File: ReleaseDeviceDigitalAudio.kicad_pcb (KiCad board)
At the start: 4 copper layers, 132 x 68.5 mm, 179 parts, among them J1 Conn_02x10_Counter_Clockwise, J2 ATMEGA_PROG, J3 SignalStrength, J4 UIBoardCON1, J5 Conn_01x04, J6 UIBoardCON2, J7 KeySwitch, Q1 BSS314PEH6327XTSA1, Q3 SQ2362ES-T1_GE3, Q4 SQD50P06-15L_GE3, U1 ATmega4809-A, U10 ULN2003F12FN-7, U11 ULN2003F12FN-7, U12 ULN2003F12FN-7, U13 ULN2003F12FN-7, U14 MAX98089ETN+, U15 SN74LV1T126, U16 SN74LV1T126, U17 BM83SM1-00TA, U18 PCF85063A, U2 VOMA617A, U3 VOMA617A, U4 LM53635LQRNL*Q1, U5 TLVH431AQDBVRQ1, U6 LM74610-Q1, U7 Compute_Module_4_Connectors, U8 CD4514BM, U9 CD4511BPWR, Y1 9HT12

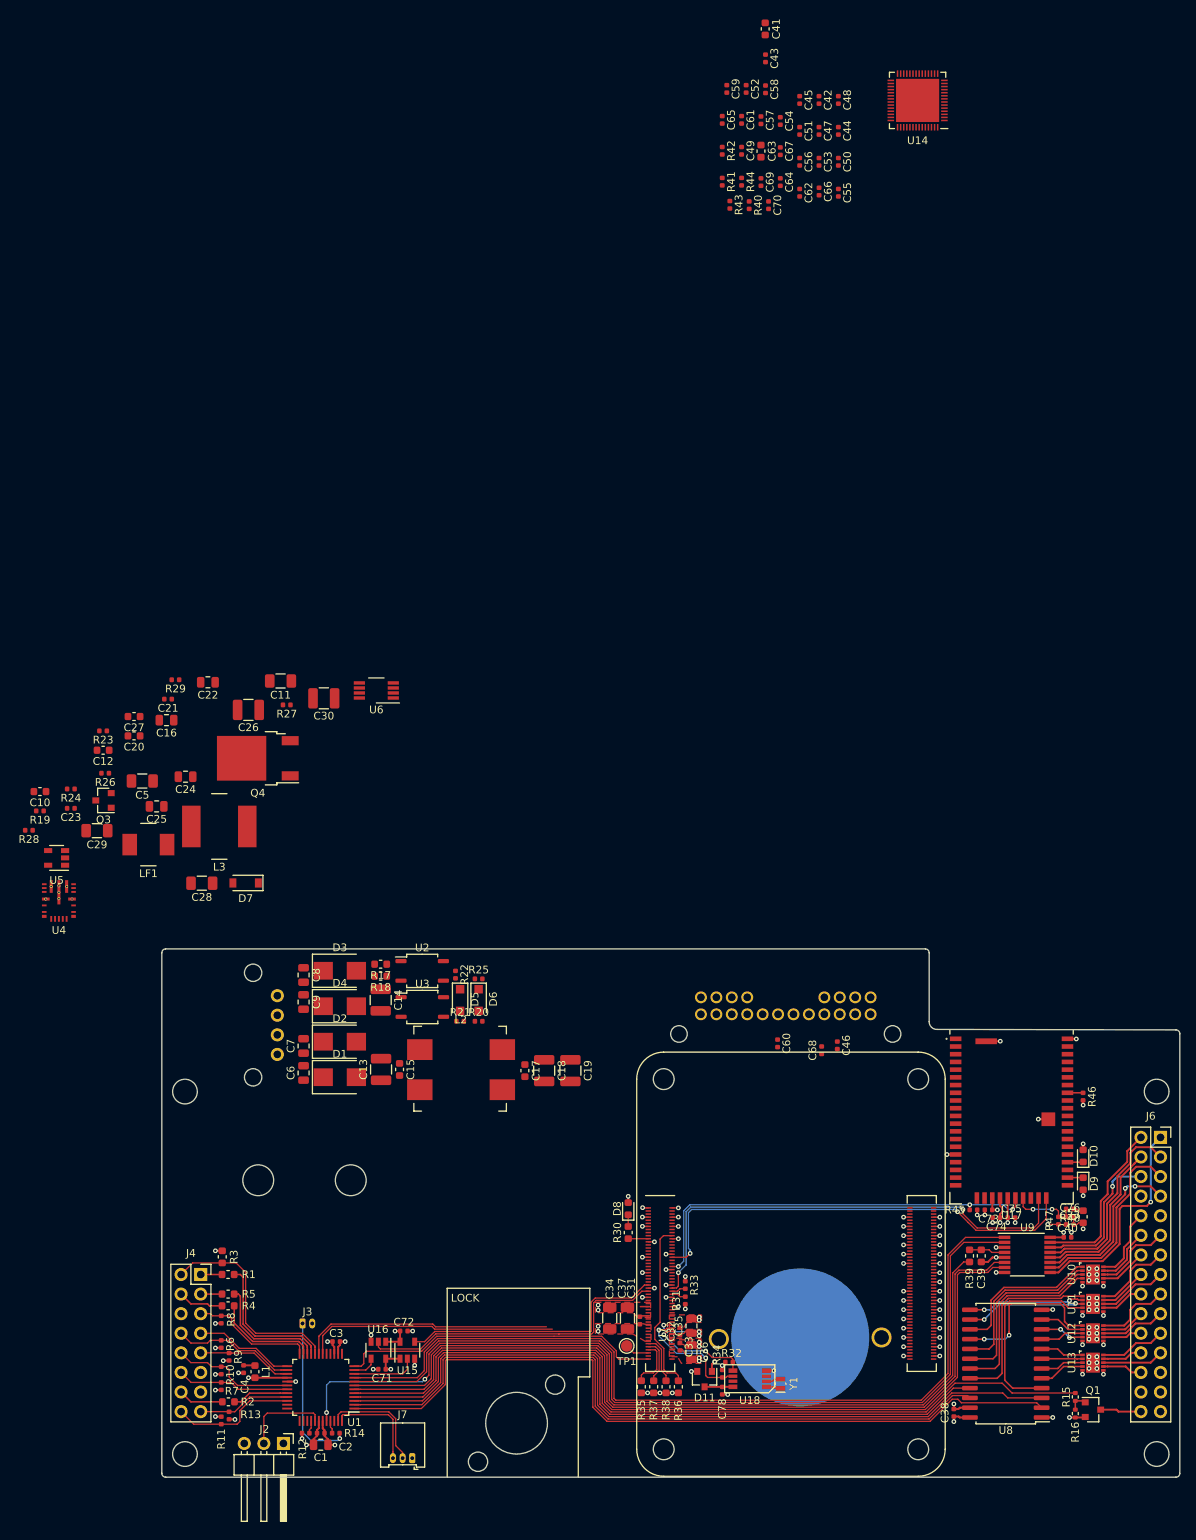
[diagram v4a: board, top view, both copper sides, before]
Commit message: - Layout MAX98 - Audiostecker Belegung angepasst
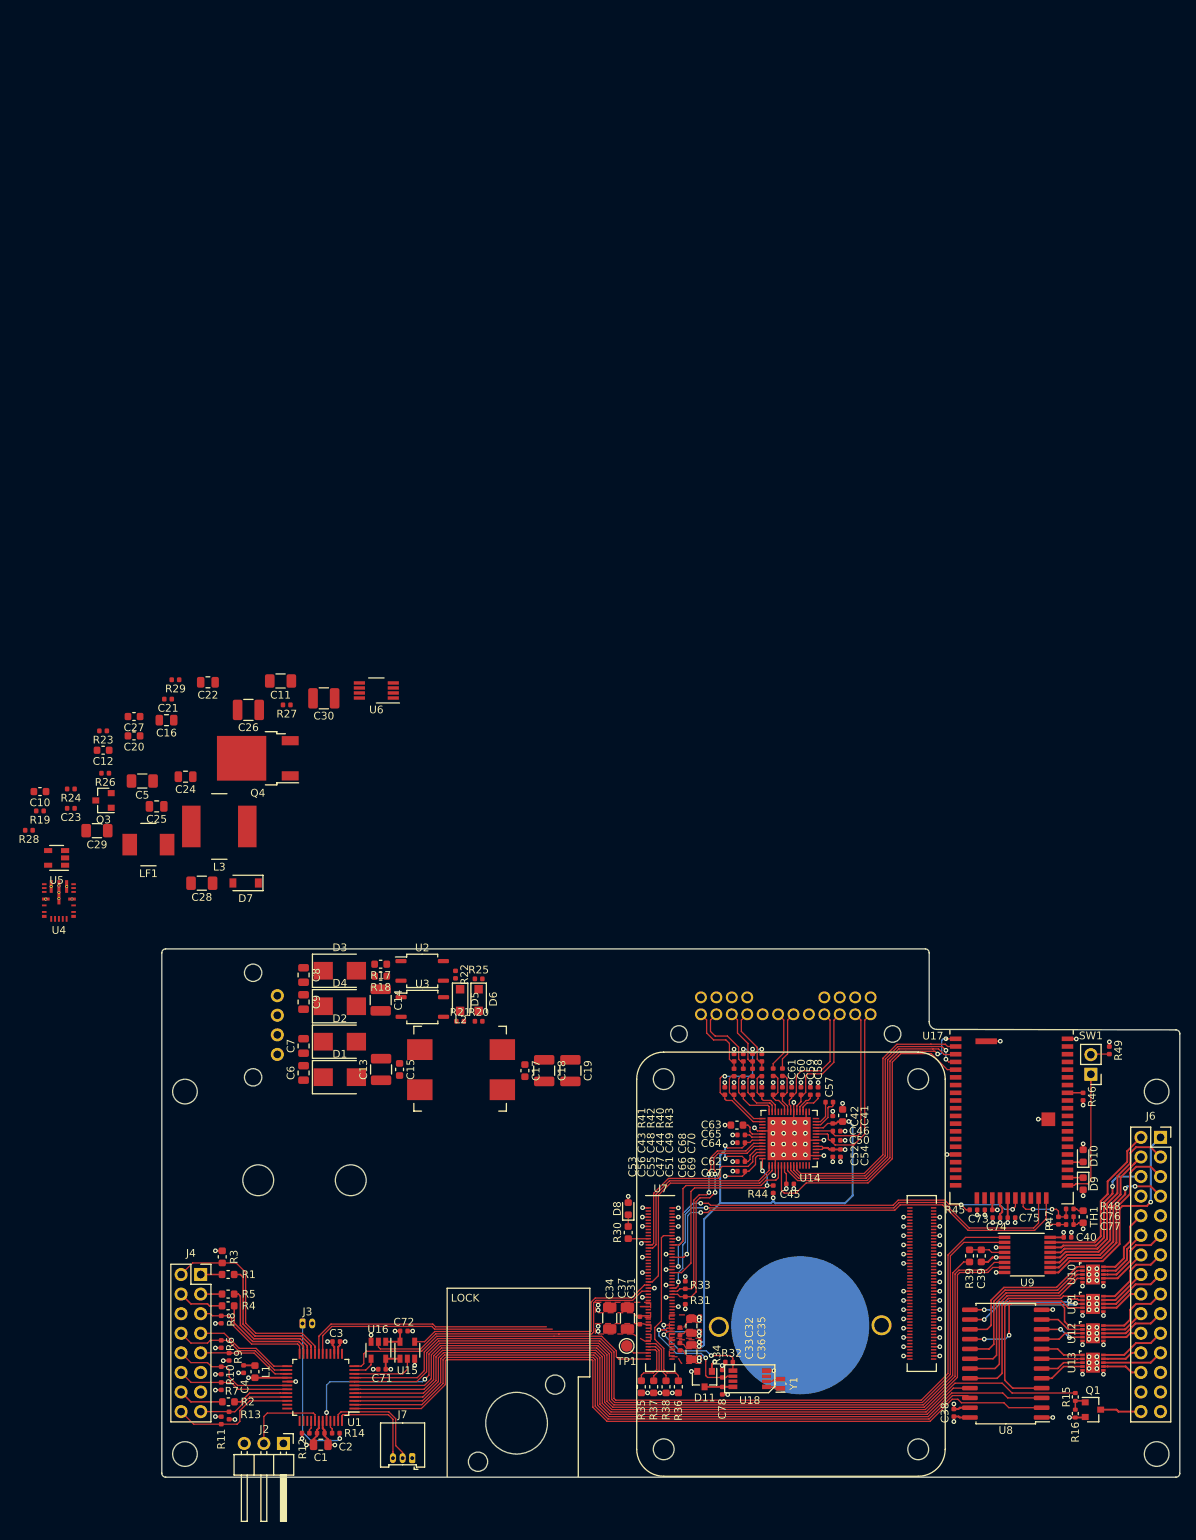
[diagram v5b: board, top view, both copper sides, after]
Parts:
- added R49: 0R, Resistor_SMD:R_0402_1005Metric, F.Cu at (206.9, 74.2)
- added SW1: SW_DIP_x01, Connector_PinHeader_2.54mm:PinHeader_1x02_P2.54mm_Vertical, F.Cu at (204.5, 77.3)
- moved C41 141.3 mm to (172.3, 82.6), turned to 90 degrees
- moved C45 140.6 mm to (165.5, 91.5), turned to 0 degrees
- moved C52 138.5 mm to (171.0, 87.5)
- moved U14 135.6 mm to (165.3, 85.6), turned to 90 degrees
- moved C54 134.1 mm to (172.0, 87.5)
- moved C67 132.4 mm to (159.1, 89.8), turned to 180 degrees
- moved C42 132.2 mm to (171.0, 83.2), turned to 90 degrees
- moved C65 131.7 mm to (159.1, 85.1), turned to 180 degrees
- moved C43 131.6 mm to (158.2, 77.0), turned to 90 degrees
- moved R44 130.7 mm to (163.3, 92.2), turned to 90 degrees
- moved C59 130.4 mm to (168.1, 79.4), turned to 90 degrees
- moved C58 130.1 mm to (169.1, 79.4), turned to 90 degrees
- moved C57 127.6 mm to (170.6, 80.9), turned to 0 degrees
- moved C50 126.9 mm to (171.5, 85.8), turned to 0 degrees
- moved C48 126.7 mm to (159.4, 77.0), turned to 90 degrees
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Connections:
- J1 pad 11: /Line_In_R -> /Audio_Handset_Out_L
- J1 pad 12: /Line_In_L -> /Audio_Handset_Out_R
- J1 pad 14: /Audio_Handset_Out_L -> /Line_In_L
- J1 pad 15: /Audio_Handset_Out_R -> /Line_In_R
- J1 pad 17: /MasterMicInN -> /HeadsetMicInP
- J1 pad 18: /MasterMicInP -> /HeadsetMicInN
- J1 pad 19: /HeadsetMicInN -> /MasterMicInP
- J1 pad 20: /HeadsetMicInP -> /MasterMicInN
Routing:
- net +1V8: track 0.00 -> 74.7 mm, vias 2 -> 6
- net /AudioMAX98089/MCLK: track 0.00 -> 41.7 mm
- net /AudioMAX98089/I2S1_SD_OUT: track 0.00 -> 39.2 mm, vias 0 -> 2
- net /AudioMAX98089/I2S1_SD_IN: track 0.00 -> 37.7 mm, vias 0 -> 2
- net /AudioMAX98089/I2S1_SD_CLK: track 0.00 -> 37.1 mm
- net /AudioMAX98089/I2S1_SD_WS: track 0.00 -> 35.8 mm
- net GND: track 85.5 -> 116.8 mm, vias 115 -> 162
- net /AudioMAX98089/I2S2_SD_CLK: track 0.00 -> 28.8 mm
- net /RPiCM4/I2C1_SDA: track 1.85 -> 29.6 mm, vias 0 -> 2
- net /RPiCM4/GPIO10: track 0.00 -> 27.0 mm, vias 0 -> 2
- net /RPiCM4/I2C1_SCL: track 1.85 -> 28.7 mm, vias 0 -> 2
- net /AudioMAX98089/I2S2_SD_IN: track 0.00 -> 24.5 mm
- net /AudioMAX98089/I2S2_SD_OUT: track 0.00 -> 24.3 mm
- net /Audio_Master_Out_R: track 0.00 -> 23.9 mm
- net /AudioMAX98089/I2S2_SD_WS: track 0.00 -> 23.0 mm
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
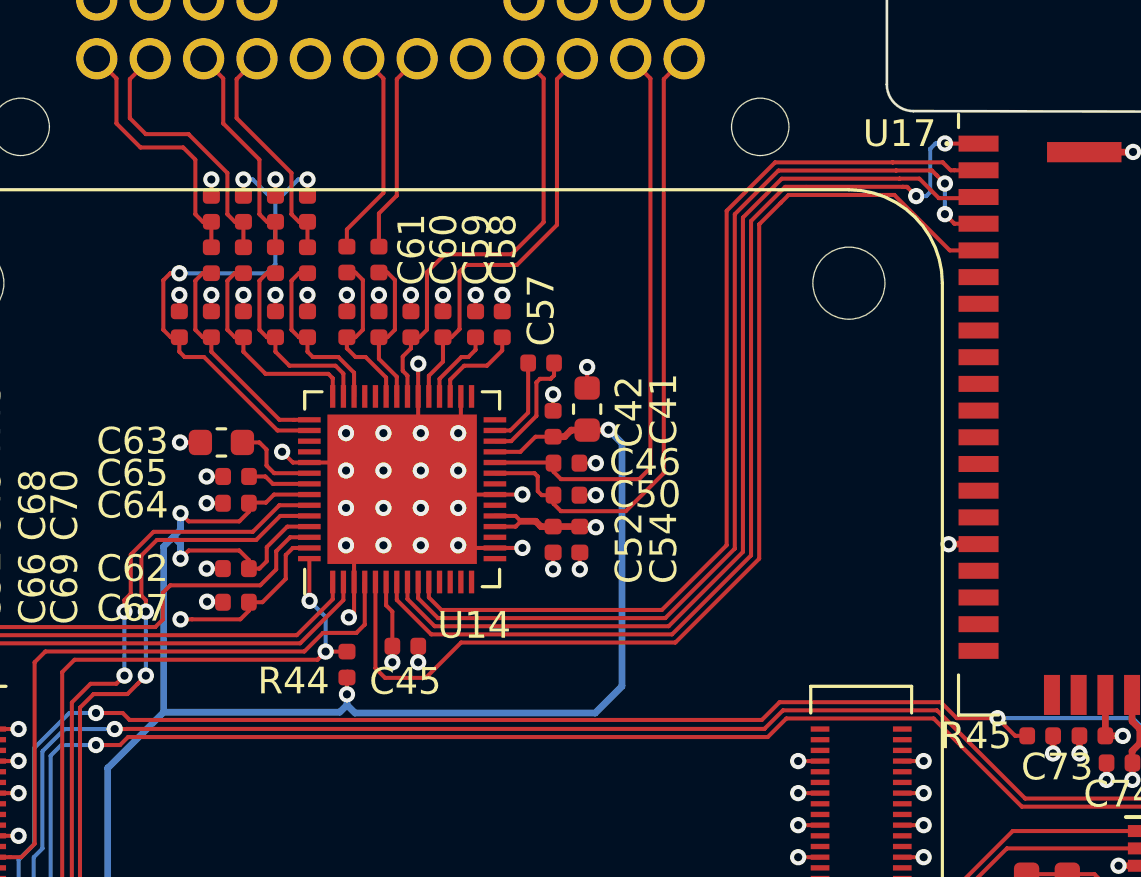
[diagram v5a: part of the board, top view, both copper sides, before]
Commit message: - IRQ Pullup Spannung auf 3,3V
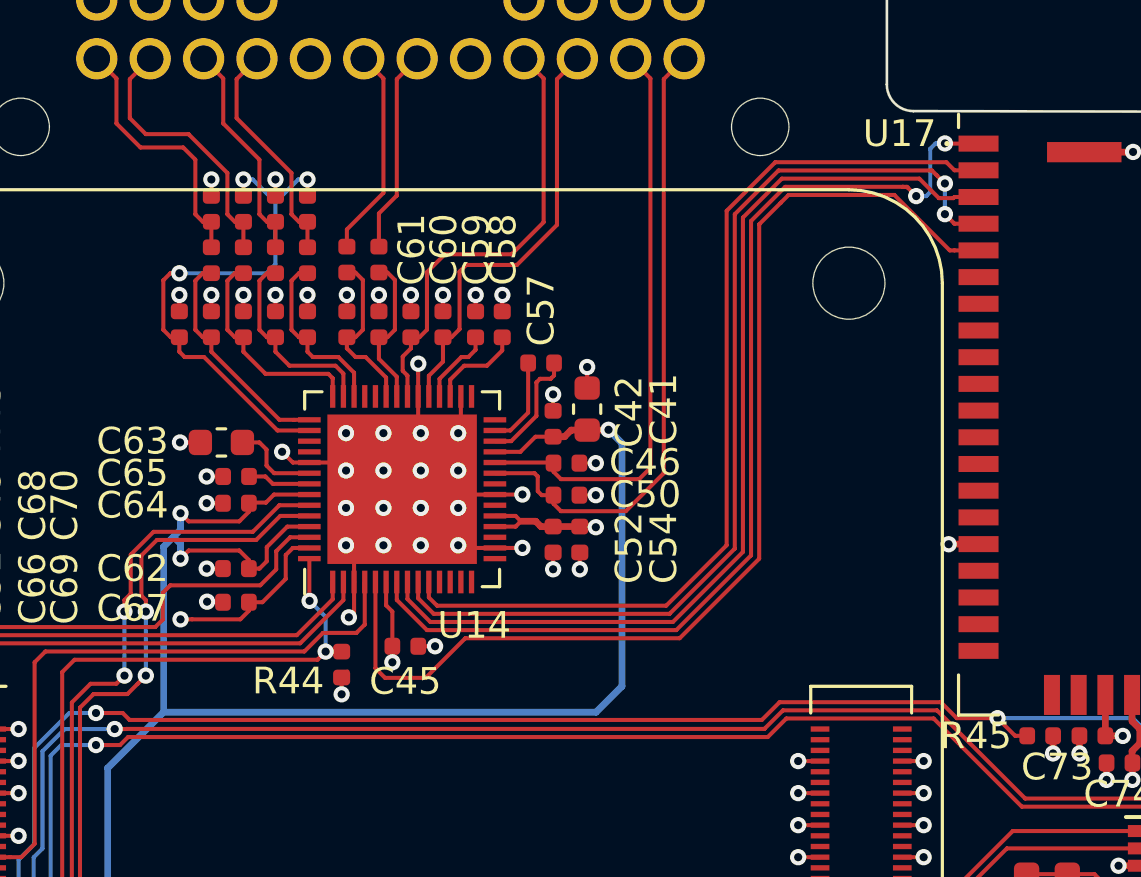
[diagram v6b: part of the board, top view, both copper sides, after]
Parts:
- moved R44 0.20 mm to (163.1, 92.2)
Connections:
- R44 pad 1: +1V8 -> +3V3
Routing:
- net +1V8: track 74.7 -> 73.2 mm, vias 6 -> 5
- net +3V3: track 31.1 -> 32.0 mm, vias 13 -> 14

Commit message: - Letzter Zwischenstand vor Branch. Alles außer Spannungsversorgung und Zündung ist vorerst fertig.
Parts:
- J2: footprint Connector_PinHeader_2.54mm:PinHeader_1x03_P2.54mm_Horizontal -> Connector_PinHeader_2.54mm:PinHeader_1x03_P2.54mm_Vertical
- R49: footprint Resistor_SMD:R_0402_1005Metric -> Resistor_SMD:R_0603_1608Metric
- moved R49 0.34 mm to (207.1, 73.9)
- renumbered SW1 to J8
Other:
- board text added: "SHORT -> TM"

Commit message: - Merged Fix for ACM1211 footprint
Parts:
- turned C17 to 90 degrees
- turned C18 to 90 degrees
- turned C19 to 90 degrees
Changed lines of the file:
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@@
     (add_net GND)
   )
+  (module TeKaDe:ACM1211 (layer F.Cu)
+    (at 122.679 76.534)
+    (fp_text reference L2 (at 0.08 -6.35) (layer F.SilkS)
+      (effects (font (size 1 1) (thickness 0.15)))
+    )
+    (fp_text value ACM1211-102-2PL-TL01 (at 0.08 -7.62) (layer F.Fab)
+      (effects (font (size 1 1) (thickness 0.15)))
+    )
+    (fp_line (start -6 5.5) (end -5 5.5) (layer F.SilkS) (width 0.12))
+    (fp_line (start -6 4.5) (end -6 5.5) (layer F.SilkS) (width 0.12))
+    (fp_line (start 6 5.5) (end 5 5.5) (layer F.SilkS) (width 0.12))
+    (fp_line (start 6 4.5) (end 6 5.5) (layer F.SilkS) (width 0.12))
+    (fp_line (start 6 -5.5) (end 6 -4.5) (layer F.SilkS) (width 0.12))
+    (fp_line (start 5 -5.5) (end 6 -5.5) (layer F.SilkS) (width 0.12))
+    (fp_line (start -6 -5.5) (end -5 -5.5) (layer F.SilkS) (width 0.12))
+    (fp_line (start -6 -4.5) (end -6 -5.5) (layer F.SilkS) (width 0.12))
+    (fp_line (start -6 5.5) (end -6 -5.5) (layer F.CrtYd) (width 0.12))
+    (fp_line (start 6 5.5) (end -6 5.5) (layer F.CrtYd) (width 0.12))
+    (fp_line (start 6 -5.5) (end 6 5.5) (layer F.CrtYd) (width 0.12))
+    (fp_line (start -6 -5.5) (end 6 -5.5) (layer F.CrtYd) (width 0.12))
+    (pad 1 smd rect (at -5.35 -2.6) (size 3.3 2.7) (layers F.Cu F.Paste F.Mask)
+      (net 26 -BATT))
+    (pad 2 smd rect (at -5.35 2.6) (size 3.3 2.7) (layers F.Cu F.Paste F.Mask)
+      (net 25 +BATT))
+    (pad 3 smd rect (at 5.35 2.6) (size 3.3 2.7) (layers F.Cu F.Paste F.Mask)
+      (net 134 "Net-(C17-Pad1)"))
+    (pad 4 smd rect (at 5.35 -2.6) (size 3.3 2.7) (layers F.Cu F.Paste F.Mask)
+      (net 2 GND))
+  )
   (module Resistor_SMD:R_0603_1608Metric (layer F.Cu)
     (at 207.079 73.884 270)
@@
       (net 1 +5V))
   )
-  (module TeKaDe:ACM1211 (layer F.Cu)
-    (at 122.679 76.534)
-    (fp_text reference L2 (at 0.08 -6.35) (layer F.SilkS)
-      (effects (font (size 1 1) (thickness 0.15)))
-    )
-    (fp_text value ACM1211-102-2PL-TL01 (at 0.08 -7.62) (layer F.Fab)
-      (effects (font (size 1 1) (thickness 0.15)))
-    )
-    (fp_line (start -6 -5.5) (end 6 -5.5) (layer F.CrtYd) (width 0.12))
-    (fp_line (start 6 -5.5) (end 6 5.5) (layer F.CrtYd) (width 0.12))
-    (fp_line (start 6 5.5) (end -6 5.5) (layer F.CrtYd) (width 0.12))
-    (fp_line (start -6 5.5) (end -6 -5.5) (layer F.CrtYd) (width 0.12))
-    (fp_line (start -6 -4.5) (end -6 -5.5) (layer F.SilkS) (width 0.12))
-    (fp_line (start -6 -5.5) (end -5 -5.5) (layer F.SilkS) (width 0.12))
-    (fp_line (start 5 -5.5) (end 6 -5.5) (layer F.SilkS) (width 0.12))
-    (fp_line (start 6 -5.5) (end 6 -4.5) (layer F.SilkS) (width 0.12))
-    (fp_line (start 6 4.5) (end 6 5.5) (layer F.SilkS) (width 0.12))
-    (fp_line (start 6 5.5) (end 5 5.5) (layer F.SilkS) (width 0.12))
-    (fp_line (start -6 4.5) (end -6 5.5) (layer F.SilkS) (width 0.12))
-    (fp_line (start -6 5.5) (end -5 5.5) (layer F.SilkS) (width 0.12))
-    (pad 1 smd rect (at -5.35 -2.6) (size 3.3 2.7) (drill (offset 0.125 0.125)) (layers F.Cu F.Paste F.Mask)
-      (net 26 -BATT))
-    (pad 2 smd rect (at -5.35 2.6) (size 3.3 2.7) (drill (offset 0.125 0.125)) (layers F.Cu F.Paste F.Mask)
-      (net 25 +BATT))
-    (pad 4 smd rect (at 5.35 2.6) (size 3.3 2.7) (drill (offset 0.125 0.125)) (layers F.Cu F.Paste F.Mask)
-      (net 2 GND))
-    (pad 3 smd rect (at 5.35 -2.6) (size 3.3 2.7) (drill (offset 0.125 0.125)) (layers F.Cu F.Paste F.Mask)
-      (net 134 "Net-(C17-Pad1)"))
-  )
   (module Diode_SMD:D_SOD-123 (layer F.Cu)
     (at 94.8664 52.45061 180)
@@
   )
   (module Capacitor_SMD:C_1210_3225Metric (layer F.Cu)
-    (at 136.979 76.784 270)
+    (at 136.979 76.784 90)
     (descr "Capacitor SMD 1210 (3225 Metric), square (rectangular) end terminal, IPC_7351 nominal, (Body size source: http://www.tortai-tech.com/upload/download/2011102023233369053.pdf), generated with kicad-footprint-generator")
     (tags capacitor)
@@
       (effects (font (size 0.8 0.8) (thickness 0.12)))
     )
-    (pad 2 smd roundrect (at 1.4 0 270) (size 1.25 2.65) (layers F.Cu F.Paste F.Mask) (roundrect_rratio 0.2)
+    (pad 2 smd roundrect (at 1.4 0 90) (size 1.25 2.65) (layers F.Cu F.Paste F.Mask) (roundrect_rratio 0.2)
       (net 2 GND))
-    (pad 1 smd roundrect (at -1.4 0 270) (size 1.25 2.65) (layers F.Cu F.Paste F.Mask) (roundrect_rratio 0.2)
+    (pad 1 smd roundrect (at -1.4 0 90) (size 1.25 2.65) (layers F.Cu F.Paste F.Mask) (roundrect_rratio 0.2)
       (net 134 "Net-(C17-Pad1)"))
     (model ${KISYS3DMOD}/Capacitor_SMD.3dshapes/C_1210_3225Metric.wrl
@@
   )
   (module Capacitor_SMD:C_1210_3225Metric (layer F.Cu)
-    (at 133.579 76.784 270)
+    (at 133.579 76.784 90)
     (descr "Capacitor SMD 1210 (3225 Metric), square (rectangular) end terminal, IPC_7351 nominal, (Body size source: http://www.tortai-tech.com/upload/download/2011102023233369053.pdf), generated with kicad-footprint-generator")
     (tags capacitor)
@@
       (effects (font (size 0.8 0.8) (thickness 0.12)))
     )
-    (pad 2 smd roundrect (at 1.4 0 270) (size 1.25 2.65) (layers F.Cu F.Paste F.Mask) (roundrect_rratio 0.2)
+    (pad 2 smd roundrect (at 1.4 0 90) (size 1.25 2.65) (layers F.Cu F.Paste F.Mask) (roundrect_rratio 0.2)
       (net 2 GND))
-    (pad 1 smd roundrect (at -1.4 0 270) (size 1.25 2.65) (layers F.Cu F.Paste F.Mask) (roundrect_rratio 0.2)
+    (pad 1 smd roundrect (at -1.4 0 90) (size 1.25 2.65) (layers F.Cu F.Paste F.Mask) (roundrect_rratio 0.2)
       (net 134 "Net-(C17-Pad1)"))
     (model ${KISYS3DMOD}/Capacitor_SMD.3dshapes/C_1210_3225Metric.wrl
@@
   )
   (module Capacitor_SMD:C_0603_1608Metric (layer F.Cu)
-    (at 131.079 76.784 270)
+    (at 131.079 76.784 90)
     (descr "Capacitor SMD 0603 (1608 Metric), square (rectangular) end terminal, IPC_7351 nominal, (Body size source: http://www.tortai-tech.com/upload/download/2011102023233369053.pdf), generated with kicad-footprint-generator")
     (tags capacitor)
@@
       (effects (font (size 0.4 0.4) (thickness 0.06)))
     )
-    (pad 2 smd roundrect (at 0.7875 0 270) (size 0.875 0.95) (layers F.Cu F.Paste F.Mask) (roundrect_rratio 0.25)
+    (pad 2 smd roundrect (at 0.7875 0 90) (size 0.875 0.95) (layers F.Cu F.Paste F.Mask) (roundrect_rratio 0.25)
       (net 2 GND))
-    (pad 1 smd roundrect (at -0.7875 0 270) (size 0.875 0.95) (layers F.Cu F.Paste F.Mask) (roundrect_rratio 0.25)
+    (pad 1 smd roundrect (at -0.7875 0 90) (size 0.875 0.95) (layers F.Cu F.Paste F.Mask) (roundrect_rratio 0.25)
       (net 134 "Net-(C17-Pad1)"))
     (model ${KISYS3DMOD}/Capacitor_SMD.3dshapes/C_0603_1608Metric.wrl
